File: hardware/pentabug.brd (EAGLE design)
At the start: 82.9 x 33 mm, 19 parts, among them IC1 ATMEGA88

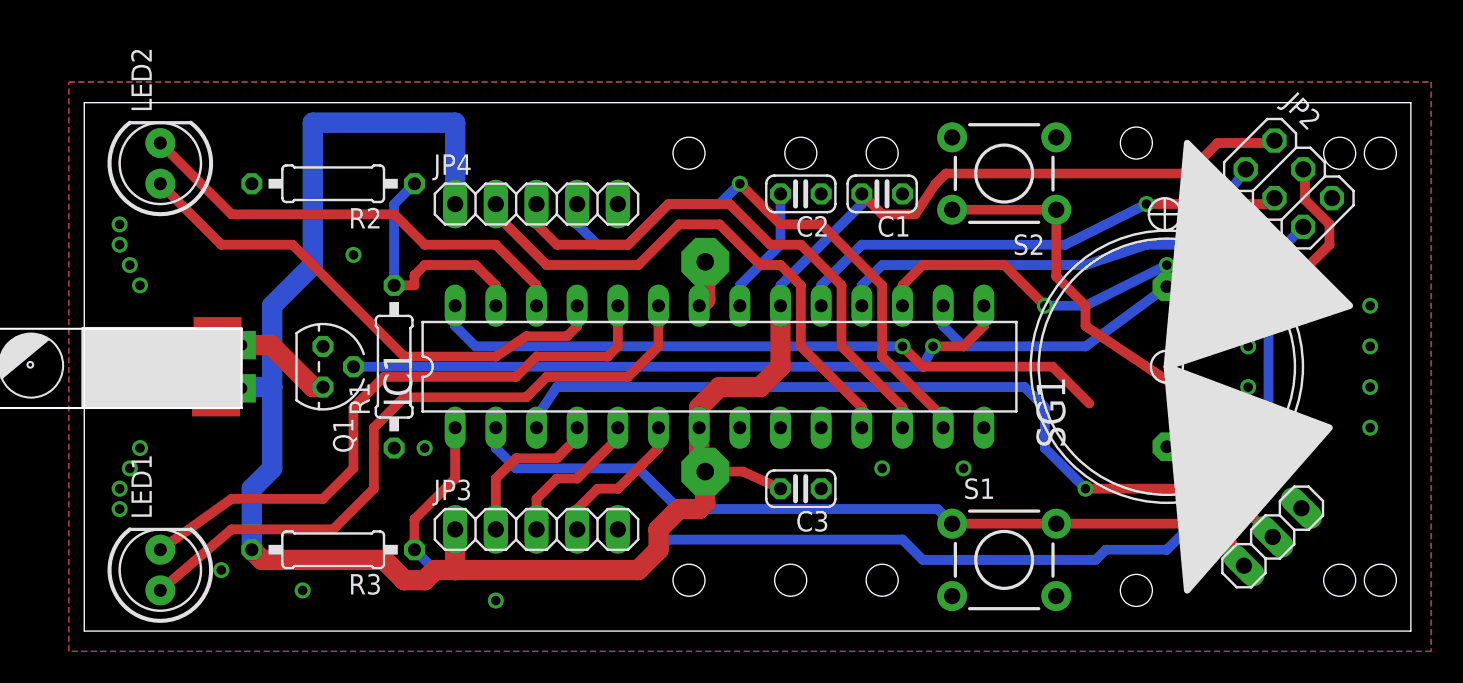
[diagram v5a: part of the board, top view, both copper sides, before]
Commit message: major routing improvents, placement und info prints
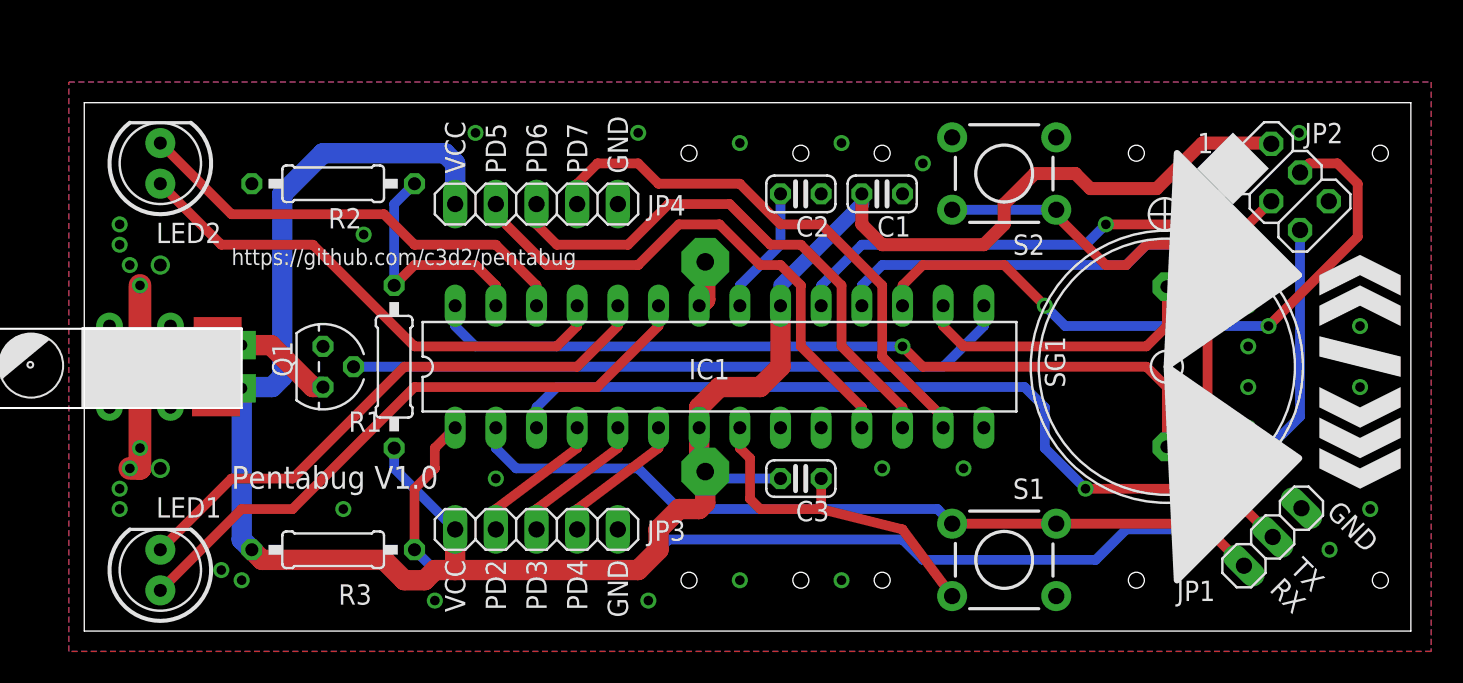
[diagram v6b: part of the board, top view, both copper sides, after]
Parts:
- moved C3 0.63 mm to (45.7, 9.53)
- moved JP2 0.28 mm to (76.0, 27.7)
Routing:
- net GND: track 2.90 -> 46.9 mm, vias 21 -> 33
- net BUZGND: track 42.9 -> 51.0 mm
- net MOSI: track 36.0 -> 41.8 mm
- net VCC: track 137.1 -> 142.5 mm
- net N$3: track 43.3 -> 39.2 mm
- net TX: track 82.0 -> 86.0 mm
- net N$10: track 38.3 -> 35.6 mm
- net BUZZR: track 17.0 -> 18.8 mm
- net PD7: track 35.5 -> 34.5 mm, vias 1 -> 0
- net PD2: track 9.94 -> 8.89 mm
- net RX: track 51.5 -> 51.0 mm
- net VIBRATE: track 42.0 -> 41.7 mm, vias 1 -> 0
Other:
- board text added: "1"
- board text added: "GND"
- board text added: "PD2"
- board text added: "PD3"
- board text added: "PD4"
- board text added: "PD5"
- board text added: "PD6"
- board text added: "PD7"
- board text added: "Pentabug V1.0"
- board text added: "RX"
- board text added: "TX"
- board text added: "VCC"
- board text added: "https://github.com/c3d2/pentabug"

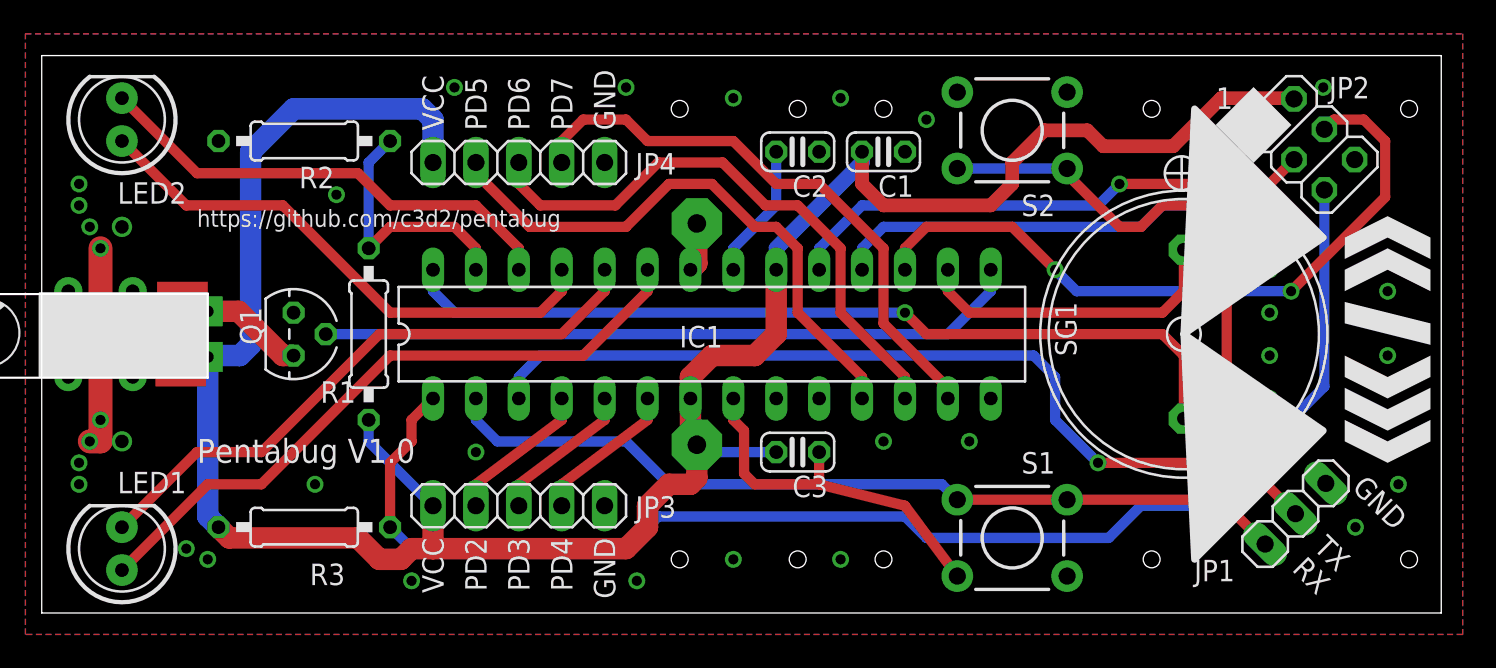
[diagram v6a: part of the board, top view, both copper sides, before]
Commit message: replaced mounting holes with big vias
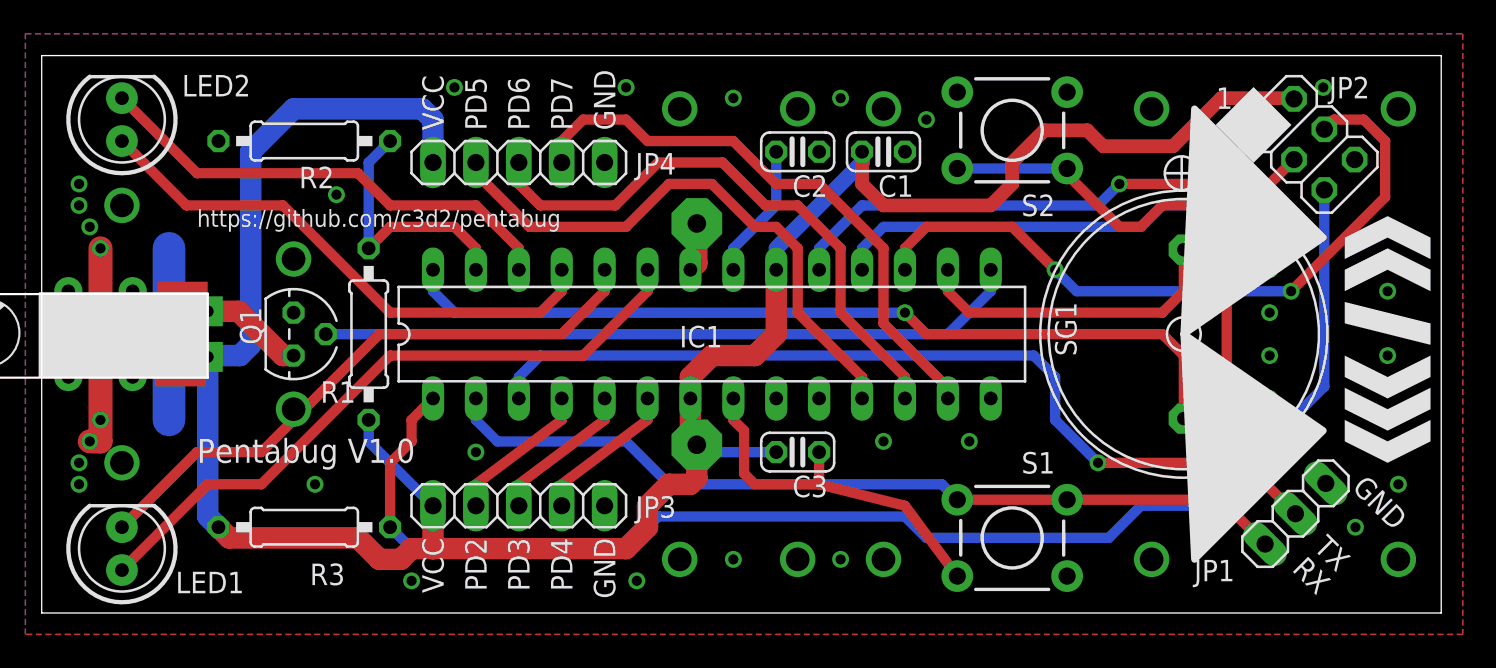
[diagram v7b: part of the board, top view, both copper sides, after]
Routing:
- net GND: track 46.9 -> 57.0 mm, vias 33 -> 43
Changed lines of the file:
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@@
 <grid distance="1.27" unitdist="mm" unit="mm" style="lines" multiple="2" display="yes" altdistance="0.635" altunitdist="mm" altunit="mm"/>
 <layers>
-<layer number="1" name="Top" color="4" fill="1" visible="yes" active="yes"/>
+<layer number="1" name="Top" color="4" fill="1" visible="no" active="yes"/>
 <layer number="2" name="Route2" color="1" fill="3" visible="no" active="no"/>
 <layer number="3" name="Route3" color="4" fill="3" visible="no" active="no"/>
@@
 <layer number="17" name="Pads" color="2" fill="1" visible="yes" active="yes"/>
 <layer number="18" name="Vias" color="2" fill="1" visible="yes" active="yes"/>
-<layer number="19" name="Unrouted" color="6" fill="1" visible="no" active="yes"/>
+<layer number="19" name="Unrouted" color="6" fill="1" visible="yes" active="yes"/>
 <layer number="20" name="Dimension" color="15" fill="1" visible="yes" active="yes"/>
 <layer number="21" name="tPlace" color="7" fill="1" visible="yes" active="yes"/>
-<layer number="22" name="bPlace" color="7" fill="1" visible="no" active="yes"/>
+<layer number="22" name="bPlace" color="7" fill="1" visible="yes" active="yes"/>
 <layer number="23" name="tOrigins" color="15" fill="1" visible="no" active="yes"/>
 <layer number="24" name="bOrigins" color="15" fill="1" visible="no" active="yes"/>
@@
 <layer number="27" name="tValues" color="7" fill="1" visible="no" active="yes"/>
 <layer number="28" name="bValues" color="7" fill="1" visible="no" active="yes"/>
-<layer number="29" name="tStop" color="7" fill="3" visible="no" active="yes"/>
+<layer number="29" name="tStop" color="7" fill="3" visible="yes" active="yes"/>
 <layer number="30" name="bStop" color="7" fill="6" visible="yes" active="yes"/>
 <layer number="31" name="tCream" color="7" fill="4" visible="no" active="yes"/>
@@
 <vertex x="69.215" y="29.845"/>
 </polygon>
-<hole x="38.735" y="3.175" drill="1"/>
-<hole x="45.72" y="29.845" drill="1"/>
-<hole x="50.8" y="29.845" drill="1"/>
-<hole x="45.72" y="3.175" drill="1"/>
-<hole x="50.8" y="3.175" drill="1"/>
-<hole x="66.675" y="3.175" drill="1"/>
-<hole x="66.675" y="29.845" drill="1"/>
-<hole x="81.915" y="29.845" drill="1"/>
-<hole x="81.915" y="3.175" drill="1"/>
-<hole x="38.735" y="29.845" drill="1"/>
 <rectangle x1="71.12" y1="27.305" x2="74.295" y2="30.48" layer="21" rot="R45"/>
 <text x="70.485" y="29.845" size="1.27" layer="25" font="vector" ratio="10">1</text>
@@
 </element>
 <element name="LED1" library="SparkFun" package="LED5MM" value="" x="5.715" y="3.81" smashed="yes" rot="R90">
-<attribute name="NAME" x="9.525" y="8.3566" size="1.27" layer="25" font="vector" ratio="10" rot="R180"/>
+<attribute name="NAME" x="8.89" y="1.1684" size="1.27" layer="25" font="vector" ratio="10"/>
 <attribute name="VALUE" x="7.5184" y="7.0104" size="1.27" layer="27" ratio="10" rot="R90"/>
 </element>
 <element name="LED2" library="SparkFun" package="LED5MM" value="" x="5.715" y="29.21" smashed="yes" rot="R90">
-<attribute name="NAME" x="9.525" y="25.5016" size="1.27" layer="25" font="vector" ratio="10" rot="R180"/>
+<attribute name="NAME" x="13.335" y="31.8516" size="1.27" layer="25" font="vector" ratio="10" rot="R180"/>
 <attribute name="VALUE" x="7.5184" y="32.4104" size="1.27" layer="27" ratio="10" rot="R90"/>
 </element>
@@
 <via x="73.66" y="17.78" extent="1-16" drill="0.6"/>
 <via x="73.66" y="20.32" extent="1-16" drill="0.6"/>
-<via x="9.525" y="3.81" extent="1-16" drill="0.6"/>
 <via x="22.86" y="1.905" extent="1-16" drill="0.6"/>
-<via x="10.795" y="3.175" extent="1-16" drill="0.6"/>
 <via x="3.175" y="7.62" extent="1-16" drill="0.6" alwaysstop="yes"/>
 <via x="3.175" y="8.89" extent="1-16" drill="0.6" alwaysstop="yes"/>
@@
 <via x="76.835" y="31.115" extent="1-16" drill="0.6"/>
 <via x="36.195" y="1.905" extent="1-16" drill="0.6"/>
-<via x="5.715" y="10.16" extent="1-16" drill="0.8" alwaysstop="yes"/>
-<via x="5.715" y="22.86" extent="1-16" drill="0.8" alwaysstop="yes"/>
+<wire x1="8.5" y1="21.59" x2="8.5" y2="11.43" width="1.9304" layer="16"/>
+<via x="5.715" y="8.89" extent="1-16" drill="1.4"/>
+<via x="5.715" y="24.13" extent="1-16" drill="1.4"/>
+<via x="38.735" y="3.175" extent="1-16" drill="1.4"/>
+<via x="45.72" y="3.175" extent="1-16" drill="1.4"/>
+<via x="50.8" y="3.175" extent="1-16" drill="1.4"/>
+<via x="66.675" y="3.175" extent="1-16" drill="1.4"/>
+<via x="81.28" y="3.175" extent="1-16" drill="1.4"/>
+<via x="81.28" y="29.845" extent="1-16" drill="1.4"/>
+<via x="66.675" y="29.845" extent="1-16" drill="1.4"/>
+<via x="45.72" y="29.845" extent="1-16" drill="1.4"/>
+<via x="50.8" y="29.845" extent="1-16" drill="1.4"/>
+<via x="38.735" y="29.845" extent="1-16" drill="1.4"/>
+<via x="15.875" y="20.955" extent="1-16" drill="1.4"/>
+<via x="15.875" y="12.065" extent="1-16" drill="1.4"/>
 </signal>
 <signal name="N$17">
@@
 </signal>
 <signal name="N$1">
-<via x="2.54" y="19.05" extent="1-16" drill="0.8" diameter="1.6764"/>
+<via x="2.54" y="19.05" extent="1-16" drill="0.8" diameter="1.6764" alwaysstop="yes"/>
 </signal>
 <signal name="N$2">
-<via x="6.35" y="19.05" extent="1-16" drill="0.8" diameter="1.6764"/>
+<via x="6.35" y="19.05" extent="1-16" drill="0.8" diameter="1.6764" alwaysstop="yes"/>
 </signal>
 <signal name="N$4">
-<via x="6.35" y="13.97" extent="1-16" drill="0.8" diameter="1.6764"/>
+<via x="6.35" y="13.97" extent="1-16" drill="0.8" diameter="1.6764" alwaysstop="yes"/>
 </signal>
 <signal name="N$6">
-<via x="2.54" y="13.97" extent="1-16" drill="0.8" diameter="1.6764"/>
+<via x="2.54" y="13.97" extent="1-16" drill="0.8" diameter="1.6764" alwaysstop="yes"/>
 </signal>
 </signals>

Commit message: minor fix
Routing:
- net GND: vias 43 -> 42
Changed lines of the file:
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@@
 <grid distance="1.27" unitdist="mm" unit="mm" style="lines" multiple="2" display="yes" altdistance="0.635" altunitdist="mm" altunit="mm"/>
 <layers>
-<layer number="1" name="Top" color="4" fill="1" visible="no" active="yes"/>
+<layer number="1" name="Top" color="4" fill="1" visible="yes" active="yes"/>
 <layer number="2" name="Route2" color="1" fill="3" visible="no" active="no"/>
 <layer number="3" name="Route3" color="4" fill="3" visible="no" active="no"/>
@@
 <via x="73.66" y="17.78" extent="1-16" drill="0.6"/>
 <via x="73.66" y="20.32" extent="1-16" drill="0.6"/>
-<via x="22.86" y="1.905" extent="1-16" drill="0.6"/>
+<via x="20.955" y="3.175" extent="1-16" drill="0.6"/>
 <via x="3.175" y="7.62" extent="1-16" drill="0.6" alwaysstop="yes"/>
 <via x="3.175" y="8.89" extent="1-16" drill="0.6" alwaysstop="yes"/>
@@
 <via x="48.26" y="3.175" extent="1-16" drill="0.6"/>
 <via x="76.835" y="31.115" extent="1-16" drill="0.6"/>
-<via x="36.195" y="1.905" extent="1-16" drill="0.6"/>
 <wire x1="8.5" y1="21.59" x2="8.5" y2="11.43" width="1.9304" layer="16"/>
 <via x="5.715" y="8.89" extent="1-16" drill="1.4"/>
